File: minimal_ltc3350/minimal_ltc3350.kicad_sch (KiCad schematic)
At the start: 85 parts, among them Q1 20.0 V, Q2 20.0 V, Q3 20 V, Q4 20 V, Q5 20.0 V, Q6 8 V, Q7 8 V, Q8 8 V, Q9 8 V, U1 LTC3350EUHF-PBF

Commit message: backup
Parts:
- added TP10, TP9: TestPoint, test_point_footprints:TestPoint_THTPad_Castelated, symbol UNITED_TEST_POINTS:TestPoint_Castelated_v2
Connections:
- net GND: now also R6.2; no longer R6.1
- net PFI: now also R6.1; no longer R6.2
- net SCL: now reaches U1.1 (SCL)
- net SCL: now also TP9.1
- net SDA: now reaches U1.2 (SDA)
- net SDA: now also TP10.1
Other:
- moved on the sheet: C1, C10, C11, C12, C13, C14, C15, C16, C17, C18, C19, C2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

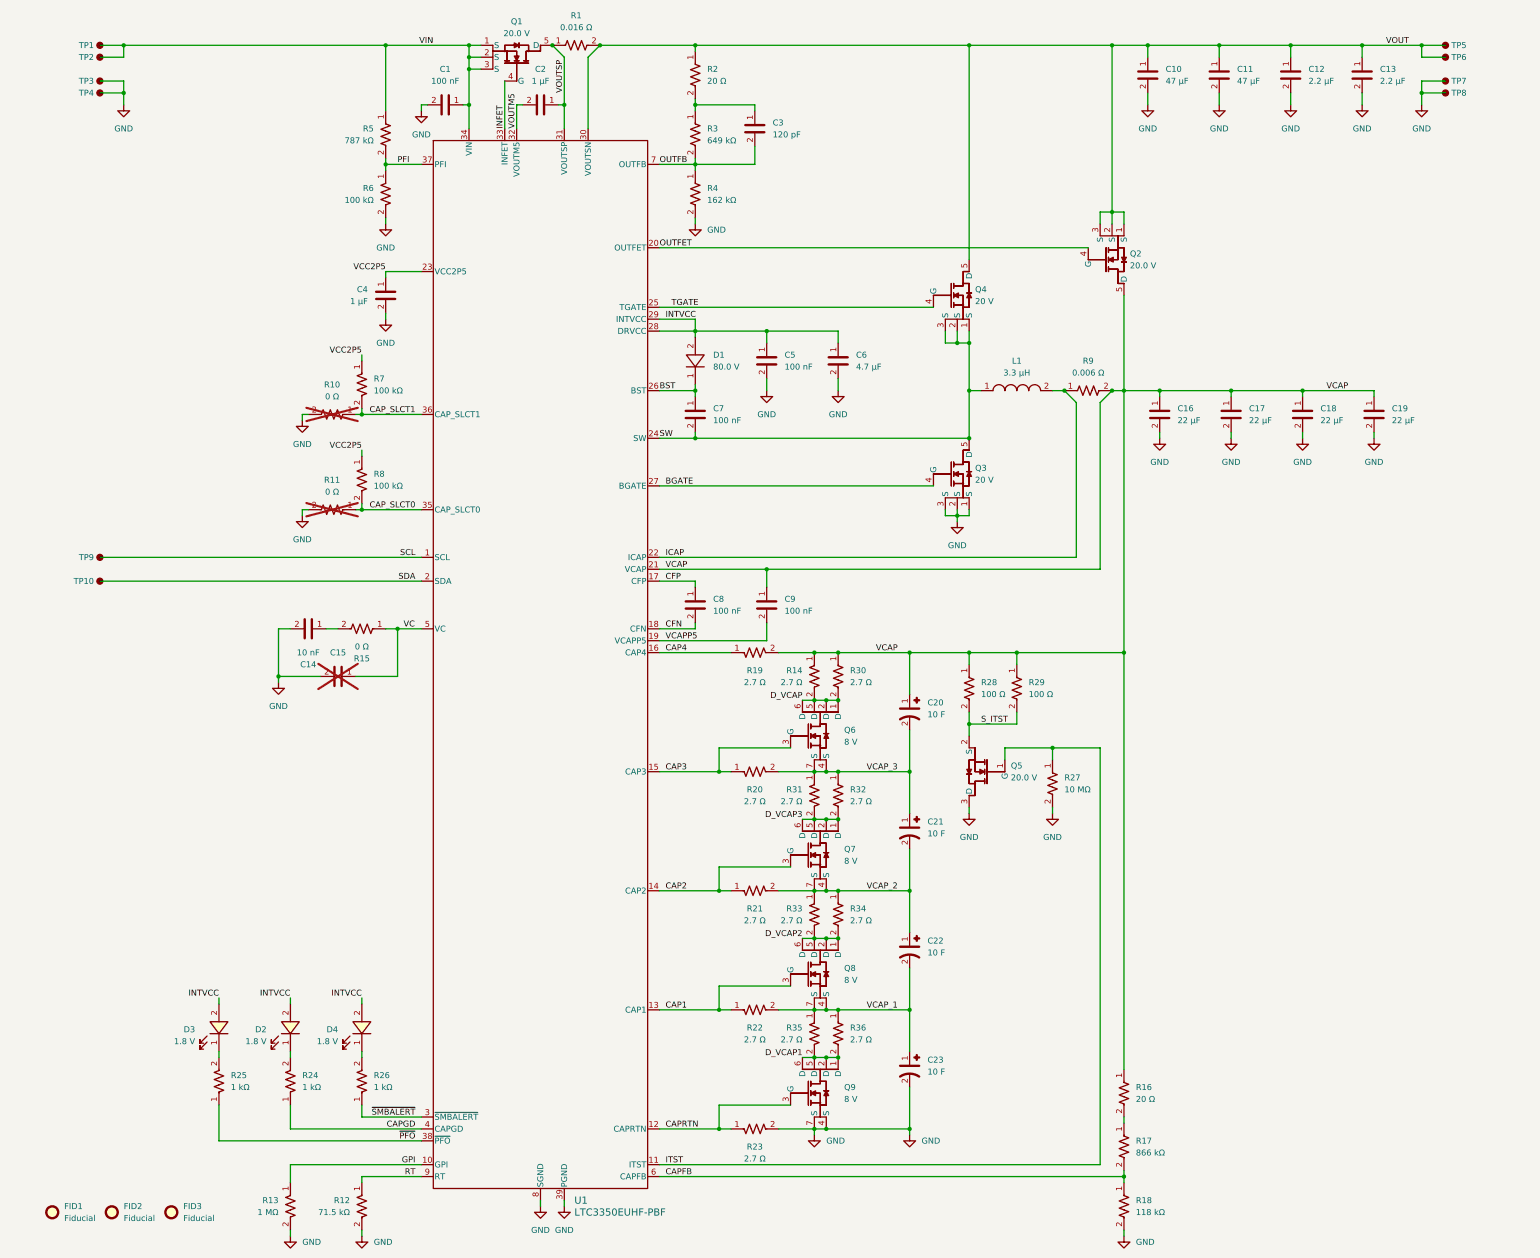
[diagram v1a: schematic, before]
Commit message: Update KiCAD files: symbols generator, schematic, and PCB layout
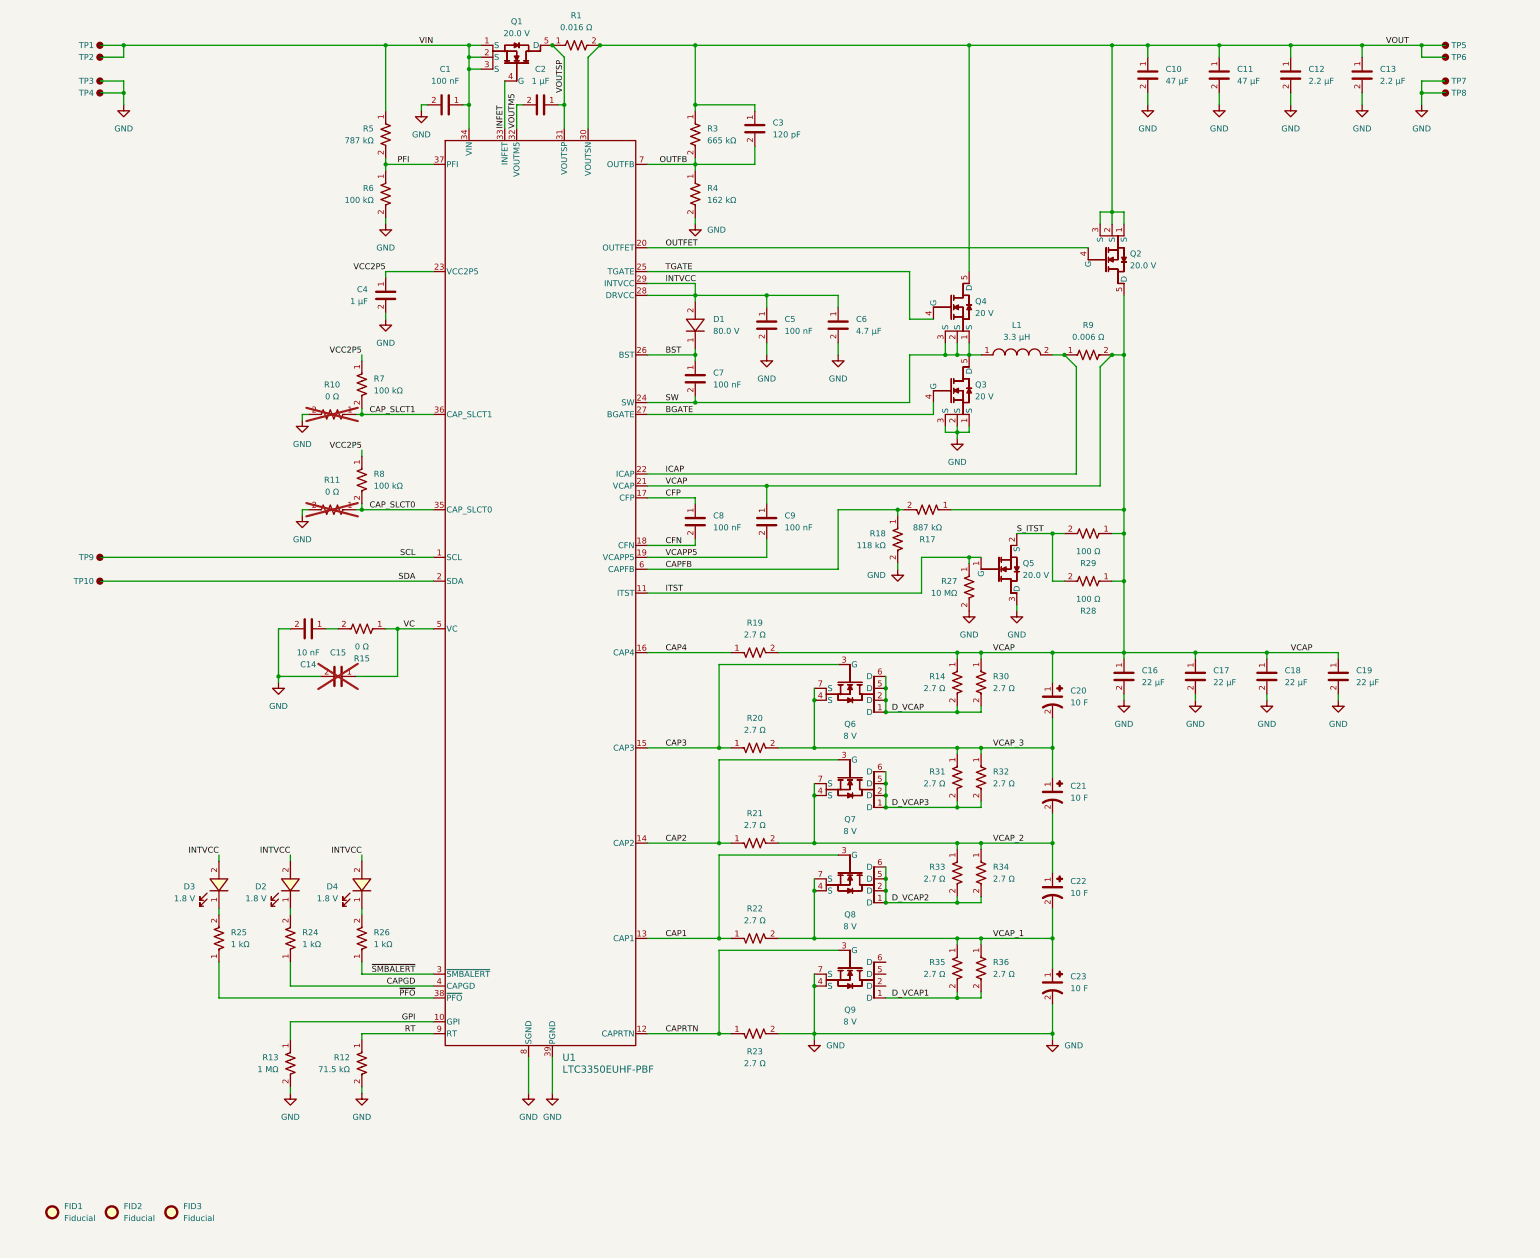
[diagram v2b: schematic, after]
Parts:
- removed R16, R2: 20 Ω, resistor_footprints:R_0402_1005Metric, symbol RESISTORS_ERJ-2RKF_DATA_BASE:R_ERJ-2RKF20R0X
- R17: value 866 kΩ -> 887 kΩ; symbol RESISTORS_ERJ-2RKF_DATA_BASE:R_ERJ-2RKF8663X -> RESISTORS_ERJ-2RKF_DATA_BASE:R_ERJ-2RKF8873X; MPN ERJ-2RKF8663X -> ERJ-2RKF8873X; Symbol Name R_ERJ-2RKF8663X -> R_ERJ-2RKF8873X; Trustedparts Search https://www.trustedparts.com/en/search/ERJ-2RKF8663X -> https://www.trustedparts.com/en/search/ERJ-2RKF8873X
- R3: value 649 kΩ -> 665 kΩ; symbol RESISTORS_ERJ-2RKF_DATA_BASE:R_ERJ-2RKF6493X -> RESISTORS_ERJ-2RKF_DATA_BASE:R_ERJ-2RKF6653X; MPN ERJ-2RKF6493X -> ERJ-2RKF6653X; Symbol Name R_ERJ-2RKF6493X -> R_ERJ-2RKF6653X; Trustedparts Search https://www.trustedparts.com/en/search/ERJ-2RKF6493X -> https://www.trustedparts.com/en/search/ERJ-2RKF6653X
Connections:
- net D_VCAP1: no longer Q9.2 (D), Q9.5 (D), Q9.6 (D)
- net VCAP: now also R17.1
- net VOUT: now also C3.1, R3.1
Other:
- moved on the sheet: C16, C17, C18, C19, C20, C21, C22, C23, C5, C6, C7, C8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

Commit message: backup
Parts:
- C20, C21, C22, C23: symbol CAPACITORS_HV08102R7_DATA_BASE:C_HV0810-2R7106-R -> CAPACITORS_HV_DATA_BASE:C_HV1030-2R7106-R; MPN HV0810-2R7106-R -> HV1030-2R7106-R; Series HV0810-2R7 -> HV1030-2R7; Symbol Name C_HV0810-2R7106-R -> C_HV1030-2R7106-R; Trustedparts Search https://www.trustedparts.com/en/search/HV0810-2R7106-R -> https://www.trustedparts.com/en/search/HV1030-2R7106-R
- Q3, Q4: symbol UNITED_TRANSISTORS_DATA_BASE:Q_BSZ060NE2LS -> TRANSISTORS_BSZ060NE2LS_DATA_BASE:Q_BSZ060NE2LS
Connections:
- net D_VCAP1: now also Q9.2 (D), Q9.5 (D), Q9.6 (D)

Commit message: Update KiCad project files
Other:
- moved on the sheet: C16, C17, C18, C19, C20, C21, C22, C23, C3, C5, C6, C7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

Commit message: docs: update KiCad files
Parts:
- C2: footprint capacitor_footprints:C_0603_1608Metric -> capacitor_footprints:C_0402_1005Metric; symbol CAPACITORS_GRM185R61E_DATA_BASE:C_GRM185R61E105KA12J -> CAPACITORS_C1005X5R1E_DATA_BASE:C_C1005X5R1E105K050BC; Case Code - in 0603 -> 0402; Case Code - mm 1608 -> 1005; MPN GRM185R61E105KA12J -> C1005X5R1E105K050BC; Manufacturer Murata Electronics -> TDK; Series GRM185R61E -> C1005X5R1E; Symbol Name C_GRM185R61E105KA12J -> C_C1005X5R1E105K050BC; Trustedparts Search https://www.trustedparts.com/en/search/GRM185R61E105KA12J -> https://www.trustedparts.com/en/search/C1005X5R1E105K050BC
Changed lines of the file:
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@@
 	)
 	(symbol
-		(lib_id "CAPACITORS_GRM185R61E_DATA_BASE:C_GRM185R61E105KA12J")
+		(lib_id "CAPACITORS_C1005X5R1E_DATA_BASE:C_C1005X5R1E105K050BC")
 		(at 137.16 35.56 0)
 		(mirror y)
@@
 			)
 		)
-		(property "Footprint" "capacitor_footprints:C_0603_1608Metric"
+		(property "Footprint" "capacitor_footprints:C_0402_1005Metric"
 			(at 137.16 43.18 0)
 			(show_name yes)
@@
 			)
 		)
-		(property "Datasheet" "https://search.murata.co.jp/Ceramy/image/img/A01X/G101/ENG/GRM185R61E105KA12-01.pdf"
+		(property "Datasheet" "https://product.tdk.com/en/search/capacitor/ceramic/mlcc/info?part_no=C1005X5R1E105K050BC"
 			(at 137.16 45.72 0)
 			(show_name yes)
@@
 			)
 		)
-		(property "Description" "CAP SMD 1 µF X5R 10% 0603 25V"
+		(property "Description" "CAP SMD 1 µF X5R 10% 0402 25V"
 			(at 137.16 48.26 0)
 			(show_name yes)
@@
 			)
 		)
-		(property "Case Code - in" "0603"
+		(property "Case Code - in" "0402"
 			(at 137.16 53.34 0)
 			(show_name yes)
@@
 			)
 		)
-		(property "Case Code - mm" "1608"
+		(property "Case Code - mm" "1005"
 			(at 137.16 55.88 0)
 			(show_name yes)
@@
 			)
 		)
-		(property "MPN" "GRM185R61E105KA12J"
+		(property "MPN" "C1005X5R1E105K050BC"
 			(at 137.16 60.96 0)
 			(show_name yes)
@@
 			)
 		)
-		(property "Manufacturer" "Murata Electronics"
+		(property "Manufacturer" "TDK"
 			(at 137.16 63.5 0)
 			(show_name yes)
@@
 			)
 		)
-		(property "Series" "GRM185R61E"
+		(property "Series" "C1005X5R1E"
 			(at 137.16 66.04 0)
 			(show_name yes)
@@
 			)
 		)
-		(property "Symbol Name" "C_GRM185R61E105KA12J"
+		(property "Symbol Name" "C_C1005X5R1E105K050BC"
 			(at 137.16 68.58 0)
 			(show_name yes)
@@
 			)
 		)
-		(property "Trustedparts Search" "https://www.trustedparts.com/en/search/GRM185R61E105KA12J"
+		(property "Trustedparts Search" "https://www.trustedparts.com/en/search/C1005X5R1E105K050BC"
 			(at 137.16 73.66 0)
 			(show_name yes)

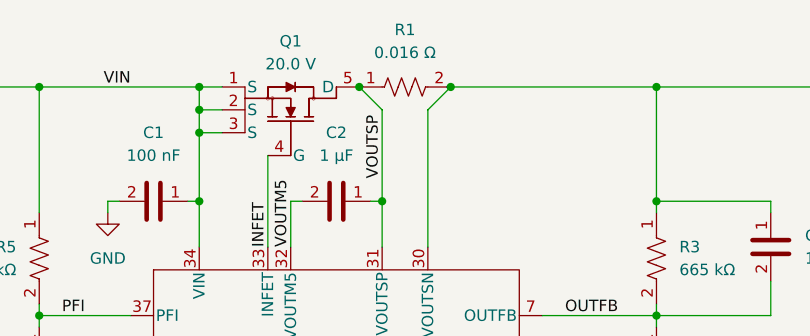
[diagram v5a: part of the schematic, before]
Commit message: feat: Update KiCad project and symbols
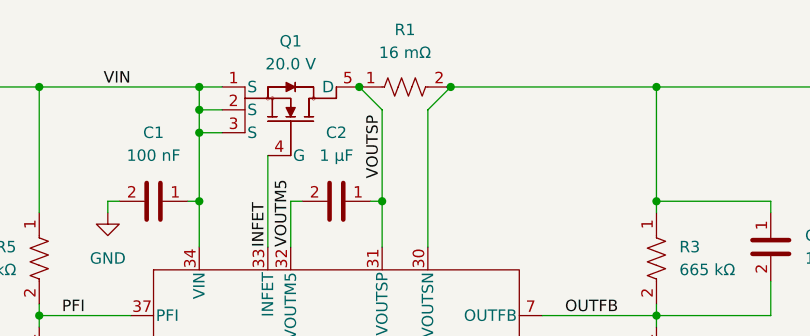
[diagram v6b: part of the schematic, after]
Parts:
- R1: value 0.016 Ω -> 16 mΩ; symbol RESISTORS_PRL1632-_DATA_BASE:R_PRL1632-R016-F-T1 -> RESISTORS_ERJ-B2CF_DATA_BASE:R_ERJ-B2CFR016V; MPN PRL1632-R016-F-T1 -> ERJ-B2CFR016V; Manufacturer Susumu -> Panasonic; Series PRL1632- -> ERJ-B2CF; Symbol Name R_PRL1632-R016-F-T1 -> R_ERJ-B2CFR016V; Trustedparts Search https://www.trustedparts.com/en/search/PRL1632-R016-F-T1 -> https://www.trustedparts.com/en/search/ERJ-B2CFR016V
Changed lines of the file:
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@@
 	)
 	(symbol
-		(lib_id "RESISTORS_PRL1632-_DATA_BASE:R_PRL1632-R016-F-T1")
+		(lib_id "RESISTORS_ERJ-B2CF_DATA_BASE:R_ERJ-B2CFR016V")
 		(at 144.78 22.86 0)
 		(unit 1)
@@
 			)
 		)
-		(property "Value" "0.016 Ω"
+		(property "Value" "16 mΩ"
 			(at 144.78 19.05 0)
 			(effects
@@
 			)
 		)
-		(property "Datasheet" "https://www.susumu.co.jp/common/pdf/n_catalog_partition07_en.pdf"
+		(property "Datasheet" "https://industrial.panasonic.com/cdbs/www-data/pdf/RDN0000/AOA0000C325.pdf"
 			(at 144.78 30.48 0)
 			(show_name yes)
@@
 			)
 		)
-		(property "Description" "RES SMD 0.016 Ω 1% 0612"
+		(property "Description" "RES SMD 16 mΩ 1% 0612"
 			(at 144.78 33.02 0)
 			(show_name yes)
@@
 			)
 		)
-		(property "MPN" "PRL1632-R016-F-T1"
+		(property "MPN" "ERJ-B2CFR016V"
 			(at 144.78 43.18 0)
 			(show_name yes)
@@
 			)
 		)
-		(property "Manufacturer" "Susumu"
+		(property "Manufacturer" "Panasonic"
 			(at 144.78 45.72 0)
 			(show_name yes)
@@
 			)
 		)
-		(property "Series" "PRL1632-"
+		(property "Series" "ERJ-B2CF"
 			(at 144.78 48.26 0)
 			(show_name yes)
@@
 			)
 		)
-		(property "Symbol Name" "R_PRL1632-R016-F-T1"
+		(property "Symbol Name" "R_ERJ-B2CFR016V"
 			(at 144.78 50.8 0)
 			(show_name yes)
@@
 			)
 		)
-		(property "Trustedparts Search" "https://www.trustedparts.com/en/search/PRL1632-R016-F-T1"
+		(property "Trustedparts Search" "https://www.trustedparts.com/en/search/ERJ-B2CFR016V"
 			(at 144.78 58.42 0)
 			(show_name yes)

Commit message: Update KiCad PCB and schematic files
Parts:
- R3: value 665 kΩ -> 909 Ω; symbol RESISTORS_ERJ-2RKF_DATA_BASE:R_ERJ-2RKF6653X -> RESISTORS_ERJ-2RKF_DATA_BASE:R_ERJ-2RKF9090X; MPN ERJ-2RKF6653X -> ERJ-2RKF9090X; Symbol Name R_ERJ-2RKF6653X -> R_ERJ-2RKF9090X; Trustedparts Search https://www.trustedparts.com/en/search/ERJ-2RKF6653X -> https://www.trustedparts.com/en/search/ERJ-2RKF9090X
- R4: value 162 kΩ -> 100 kΩ; symbol RESISTORS_ERJ-2RKF_DATA_BASE:R_ERJ-2RKF1623X -> RESISTORS_ERJ-2RKF_DATA_BASE:R_ERJ-2RKF1003X; MPN ERJ-2RKF1623X -> ERJ-2RKF1003X; Symbol Name R_ERJ-2RKF1623X -> R_ERJ-2RKF1003X; Trustedparts Search https://www.trustedparts.com/en/search/ERJ-2RKF1623X -> https://www.trustedparts.com/en/search/ERJ-2RKF1003X
- R9: value 0.006 Ω -> 6 mΩ; symbol RESISTORS_PRL1632-_DATA_BASE:R_PRL1632-R006-F-T1 -> RESISTORS_WFCP0612_DATA_BASE:R_WFCP06126L000FE66; MPN PRL1632-R006-F-T1 -> WFCP06126L000FE66; Manufacturer Susumu -> Vishay; Series PRL1632- -> WFCP0612; Symbol Name R_PRL1632-R006-F-T1 -> R_WFCP06126L000FE66; Trustedparts Search https://www.trustedparts.com/en/search/PRL1632-R006-F-T1 -> https://www.trustedparts.com/en/search/WFCP06126L000FE66
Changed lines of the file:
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@@
 	)
 	(symbol
-		(lib_id "RESISTORS_ERJ-2RKF_DATA_BASE:R_ERJ-2RKF1623X")
+		(lib_id "RESISTORS_ERJ-2RKF_DATA_BASE:R_ERJ-2RKF1003X")
 		(at 172.72 54.61 270)
 		(unit 1)
@@
 		(on_board yes)
 		(dnp no)
+		(fields_autoplaced yes)
 		(property "Reference" "R4"
 			(at 175.26 53.3399 90)
@@
 			)
 		)
-		(property "Value" "162 kΩ"
+		(property "Value" "100 kΩ"
 			(at 175.26 55.8799 90)
 			(effects
@@
 			)
 		)
-		(property "Description" "RES SMD 162 kΩ 1% 0402 50V"
+		(property "Description" "RES SMD 100 kΩ 1% 0402 50V"
 			(at 162.56 54.61 0)
 			(show_name yes)
@@
 			)
 		)
-		(property "MPN" "ERJ-2RKF1623X"
+		(property "MPN" "ERJ-2RKF1003X"
 			(at 152.4 54.61 0)
 			(show_name yes)
@@
 			)
 		)
-		(property "Symbol Name" "R_ERJ-2RKF1623X"
+		(property "Symbol Name" "R_ERJ-2RKF1003X"
 			(at 144.78 54.61 0)
 			(show_name yes)
@@
 			)
 		)
-		(property "Trustedparts Search" "https://www.trustedparts.com/en/search/ERJ-2RKF1623X"
+		(property "Trustedparts Search" "https://www.trustedparts.com/en/search/ERJ-2RKF1003X"
 			(at 137.16 54.61 0)
 			(show_name yes)
@@
 	)
 	(symbol
-		(lib_id "RESISTORS_PRL1632-_DATA_BASE:R_PRL1632-R006-F-T1")
+		(lib_id "RESISTORS_WFCP0612_DATA_BASE:R_WFCP06126L000FE66")
 		(at 254 88.9 0)
 		(unit 1)
@@
 			)
 		)
-		(property "Value" "0.006 Ω"
+		(property "Value" "6 mΩ"
 			(at 254 85.09 0)
 			(effects
@@
 			)
 		)
-		(property "Datasheet" "https://www.susumu.co.jp/common/pdf/n_catalog_partition07_en.pdf"
+		(property "Datasheet" "https://industrial.panasonic.com/cdbs/www-data/pdf/RDN0000/AOA0000C325.pdf"
 			(at 254 96.52 0)
 			(show_name yes)
@@
 			)
 		)
-		(property "Description" "RES SMD 0.006 Ω 1% 0612"
+		(property "Description" "RES SMD 6 mΩ 1% 0612"
 			(at 254 99.06 0)
 			(show_name yes)
@@
 			)
 		)
-		(property "MPN" "PRL1632-R006-F-T1"
+		(property "MPN" "WFCP06126L000FE66"
 			(at 254 109.22 0)
 			(show_name yes)
@@
 			)
 		)
-		(property "Manufacturer" "Susumu"
+		(property "Manufacturer" "Vishay"
 			(at 254 111.76 0)
 			(show_name yes)
@@
 			)
 		)
-		(property "Series" "PRL1632-"
+		(property "Series" "WFCP0612"
 			(at 254 114.3 0)
 			(show_name yes)
@@
 			)
 		)
-		(property "Symbol Name" "R_PRL1632-R006-F-T1"
+		(property "Symbol Name" "R_WFCP06126L000FE66"
 			(at 254 116.84 0)
 			(show_name yes)
@@
 			)
 		)
-		(property "Trustedparts Search" "https://www.trustedparts.com/en/search/PRL1632-R006-F-T1"
+		(property "Trustedparts Search" "https://www.trustedparts.com/en/search/WFCP06126L000FE66"
 			(at 254 124.46 0)
 			(show_name yes)
@@
 	)
 	(symbol
-		(lib_id "RESISTORS_ERJ-2RKF_DATA_BASE:R_ERJ-2RKF6653X")
+		(lib_id "RESISTORS_ERJ-2RKF_DATA_BASE:R_ERJ-2RKF9090X")
 		(at 172.72 41.91 270)
 		(unit 1)
@@
 			)
 		)
-		(property "Value" "665 kΩ"
+		(property "Value" "909 Ω"
 			(at 175.26 43.1799 90)
 			(effects
@@
 			)
 		)
-		(property "Description" "RES SMD 665 kΩ 1% 0402 50V"
+		(property "Description" "RES SMD 909 Ω 1% 0402 50V"
 			(at 162.56 41.91 0)
 			(show_name yes)
@@
 			)
 		)
-		(property "MPN" "ERJ-2RKF6653X"
+		(property "MPN" "ERJ-2RKF9090X"
 			(at 152.4 41.91 0)
 			(show_name yes)
@@
 			)
 		)
-		(property "Symbol Name" "R_ERJ-2RKF6653X"
+		(property "Symbol Name" "R_ERJ-2RKF9090X"
 			(at 144.78 41.91 0)
 			(show_name yes)
@@
 			)
 		)
-		(property "Trustedparts Search" "https://www.trustedparts.com/en/search/ERJ-2RKF6653X"
+		(property "Trustedparts Search" "https://www.trustedparts.com/en/search/ERJ-2RKF9090X"
 			(at 137.16 41.91 0)
 			(show_name yes)

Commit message: Update KiCad schematic and PCB files
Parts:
- added J1, J2, J3, J4, J5: CLP-102-02-G-D-BE, connector_footprints:CLP-102-02-G-D-BE, symbol CONNECTORS_CLP-1xx-02-G-D-BE_DATA_BASE:J_CLP-102-02-G-D-BE
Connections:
- net GND: now also J5.1, J5.2, J5.3, J5.4
- net VCAP: now also J1.1, J1.2, J1.3, J1.4
- net VCAP_1: now also J4.1, J4.2, J4.3, J4.4
- net VCAP_2: now also J3.1, J3.2, J3.3, J3.4
- net VCAP_3: now also J2.1, J2.2, J2.3, J2.4
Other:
- moved on the sheet: C16, C17, C18, C19, C20, C21, C22, C23
